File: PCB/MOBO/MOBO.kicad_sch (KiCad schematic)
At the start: 5 parts, among them J103 RPi_GPio, J104 RPi_GND, J105 RPi_5V, J106 RPi_DM, J107 RPi_DM

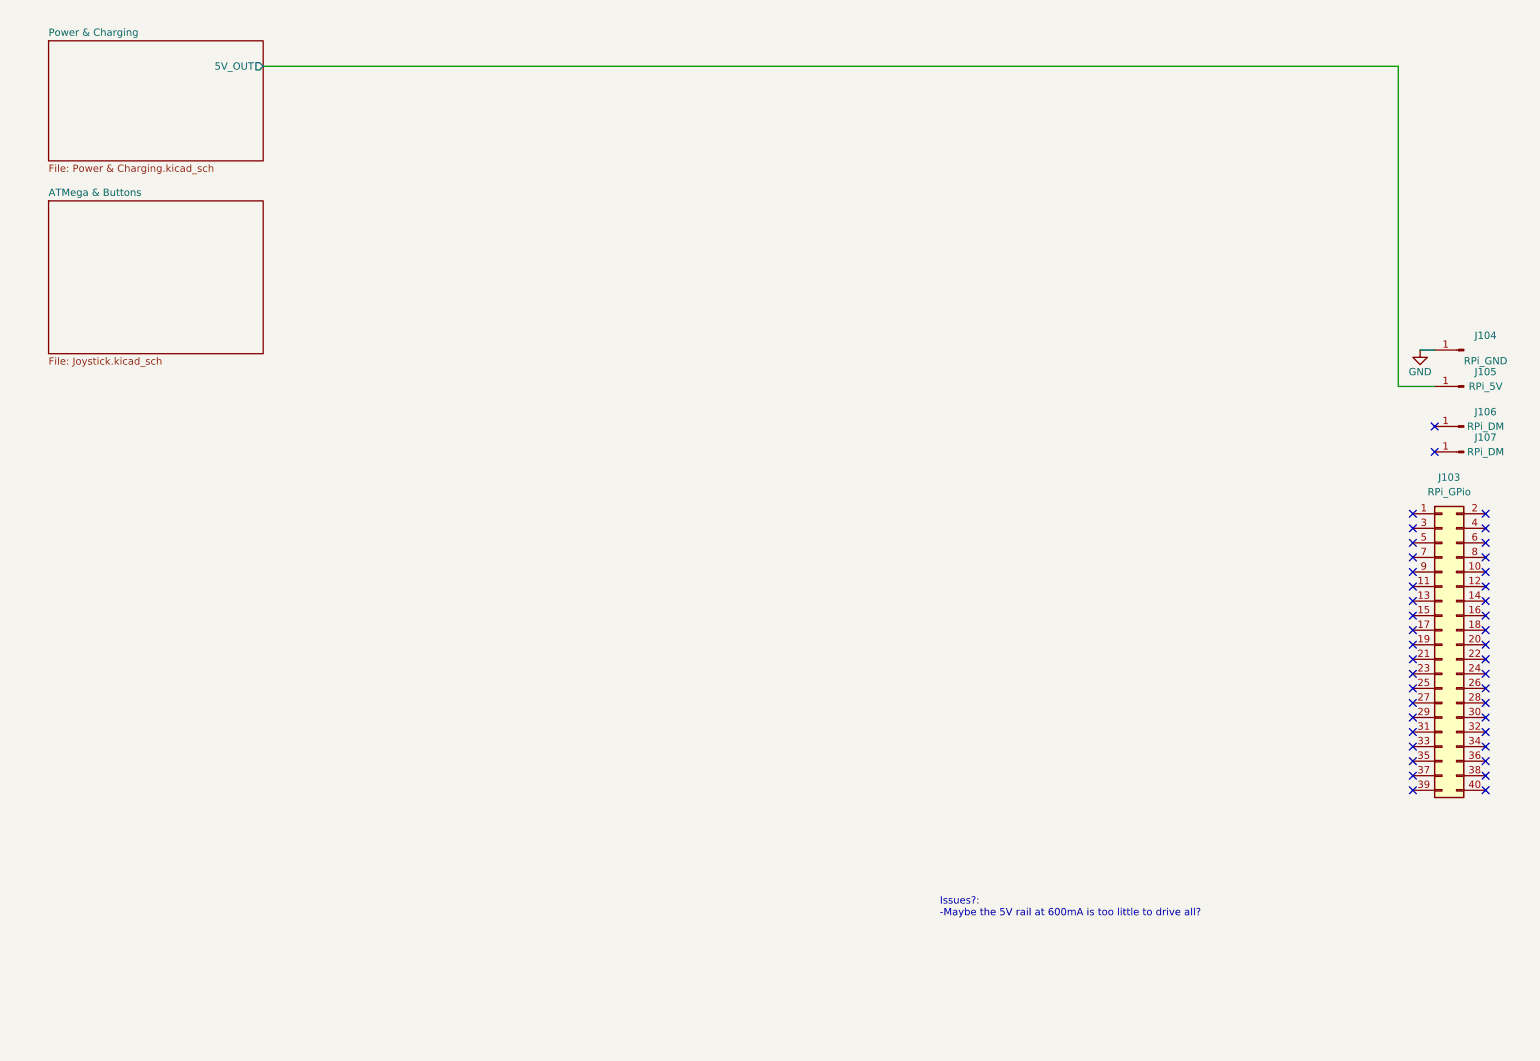
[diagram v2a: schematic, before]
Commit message: added all joystick buttons
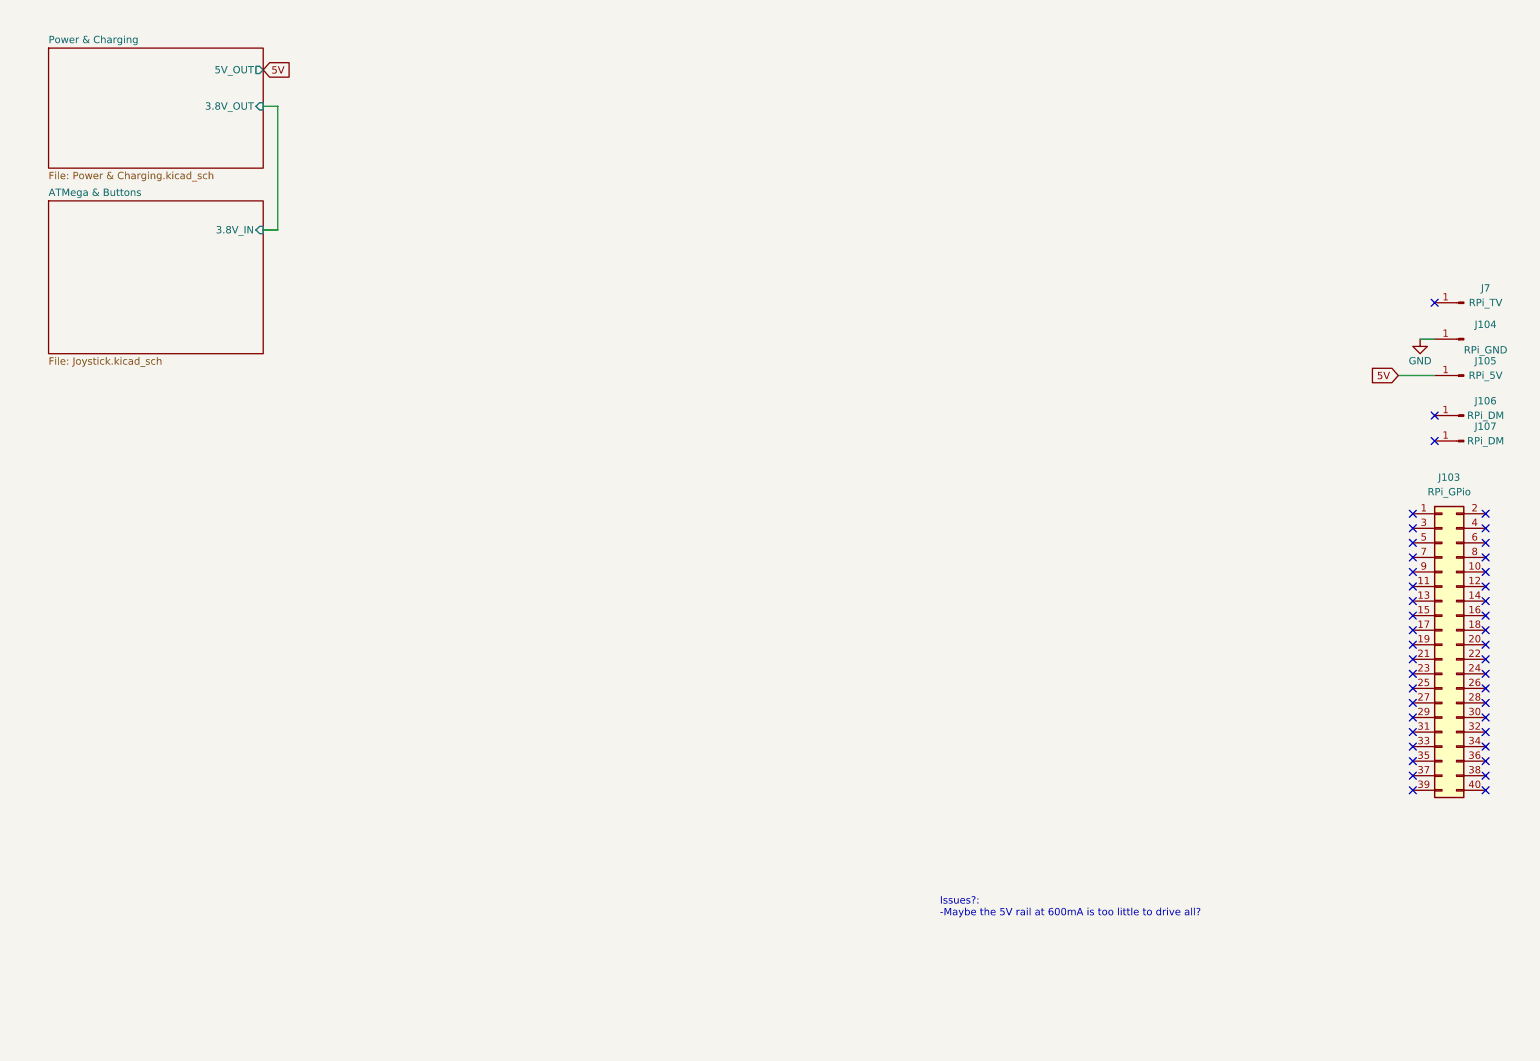
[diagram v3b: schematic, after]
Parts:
- added J7: RPi_TV, TestPoint:TestPoint_Pad_1.5x1.5mm, symbol Connector:Conn_01x01_Male
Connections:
- net Power & Charging/5V_OUT renamed 5V
- no-connect marks 42 -> 43
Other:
- sheet ATMega & Buttons ports: added 3.8V_IN; removed none
- sheet Power & Charging ports: added 3.8V_OUT; removed none
- moved on the sheet: J104, J105, J106, J107
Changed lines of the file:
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@@
   (no_connect (at 260.35 107.95))
   (no_connect (at 260.35 135.89))
-  (no_connect (at 264.16 89.535))
+  (no_connect (at 264.16 87.63))
   (no_connect (at 273.05 135.89))
   (no_connect (at 260.35 125.73))
@@
   (no_connect (at 260.35 146.05))
   (no_connect (at 260.35 113.03))
-  (no_connect (at 264.16 85.09))
+  (no_connect (at 264.16 83.185))
   (no_connect (at 260.35 143.51))
   (no_connect (at 260.35 140.97))
@@
   (no_connect (at 273.05 120.65))
   (no_connect (at 260.35 102.87))
+  (no_connect (at 264.16 63.5))
   (no_connect (at 273.05 140.97))
   (no_connect (at 260.35 115.57))
@@
   (no_connect (at 273.05 148.59))
   (no_connect (at 273.05 102.87))
-  (wire (pts (xy 257.81 22.225) (xy 257.81 78.105))
-    (stroke (width 0) (type default))
-  )
-  (wire (pts (xy 261.62 71.755) (xy 264.16 71.755))
-    (stroke (width 0) (type default))
-  )
-  (wire (pts (xy 59.69 22.225) (xy 257.81 22.225))
-    (stroke (width 0) (type default))
-  )
-  (wire (pts (xy 257.81 78.105) (xy 264.16 78.105))
+  (wire (pts (xy 59.69 29.21) (xy 62.23 29.21))
+    (stroke (width 0) (type default))
+  )
+  (wire (pts (xy 62.23 50.8) (xy 59.69 50.8))
+    (stroke (width 0) (type default))
+  )
+  (wire (pts (xy 261.62 69.85) (xy 264.16 69.85))
+    (stroke (width 0) (type default))
+  )
+  (wire (pts (xy 62.23 29.21) (xy 62.23 50.8))
+    (stroke (width 0) (type default))
+  )
+  (wire (pts (xy 257.81 76.2) (xy 264.16 76.2))
     (stroke (width 0) (type default))
   )
@@
     (at 177.8 170.815 0)
     (effects (font (size 1.27 1.27)) (justify left bottom))
+  )
+  (global_label "5V" (shape input) (at 59.69 22.86 0) (fields_autoplaced)
+    (effects (font (size 1.27 1.27)) (justify left))
+    (property "Intersheetrefs" "${INTERSHEET_REFS}" (at 64.9733 22.86 0)
+      (effects (font (size 1.27 1.27)) (justify left) hide)
+    )
+  )
+  (global_label "5V" (shape input) (at 257.81 76.2 180) (fields_autoplaced)
+    (effects (font (size 1.27 1.27)) (justify right))
+    (property "Intersheetrefs" "${INTERSHEET_REFS}" (at 252.5267 76.2 0)
+      (effects (font (size 1.27 1.27)) (justify right) hide)
+    )
+  )
+  (symbol (lib_id "Connector:Conn_01x01_Male") (at 269.24 63.5 180) (unit 1)
+    (in_bom yes) (on_board yes) (dnp no)
+    (property "Reference" "J7" (at 273.05 60.96 0)
+      (effects (font (size 1.27 1.27)))
+    )
+    (property "Value" "RPi_TV" (at 273.05 63.5 0)
+      (effects (font (size 1.27 1.27)))
+    )
+    (property "Footprint" "TestPoint:TestPoint_Pad_1.5x1.5mm" (at 269.24 63.5 0)
+      (effects (font (size 1.27 1.27)) hide)
+    )
+    (property "Datasheet" "~" (at 269.24 63.5 0)
+      (effects (font (size 1.27 1.27)) hide)
+    )
+    (pin "1")
+    (instances
+      (project "MOBO"
+        (path "/2d62a3c1-c4f2-4921-9f6b-8dc8aef69d64"
+          (reference "J7") (unit 1)
+        )
+      )
+    )
   )
   (symbol (lib_id "Connector_Generic:Conn_02x20_Odd_Even") (at 265.43 123.19 0) (unit 1)
@@
     )
   )
-  (symbol (lib_id "Connector:Conn_01x01_Male") (at 269.24 71.755 180) (unit 1)
-    (in_bom yes) (on_board yes) (dnp no)
-    (property "Reference" "J104" (at 273.05 69.215 0)
-      (effects (font (size 1.27 1.27)))
-    )
-    (property "Value" "RPi_GND" (at 273.05 73.66 0)
-      (effects (font (size 1.27 1.27)))
-    )
-    (property "Footprint" "TestPoint:TestPoint_Pad_1.5x1.5mm" (at 269.24 71.755 0)
-      (effects (font (size 1.27 1.27)) hide)
-    )
-    (property "Datasheet" "~" (at 269.24 71.755 0)
+  (symbol (lib_id "Connector:Conn_01x01_Male") (at 269.24 69.85 180) (unit 1)
+    (in_bom yes) (on_board yes) (dnp no)
+    (property "Reference" "J104" (at 273.05 67.31 0)
+      (effects (font (size 1.27 1.27)))
+    )
+    (property "Value" "RPi_GND" (at 273.05 71.755 0)
+      (effects (font (size 1.27 1.27)))
+    )
+    (property "Footprint" "TestPoint:TestPoint_Pad_1.5x1.5mm" (at 269.24 69.85 0)
+      (effects (font (size 1.27 1.27)) hide)
+    )
+    (property "Datasheet" "~" (at 269.24 69.85 0)
       (effects (font (size 1.27 1.27)) hide)
     )
@@
     )
   )
-  (symbol (lib_id "Connector:Conn_01x01_Male") (at 269.24 89.535 180) (unit 1)
-    (in_bom yes) (on_board yes) (dnp no)
-    (property "Reference" "J107" (at 273.05 86.995 0)
-      (effects (font (size 1.27 1.27)))
-    )
-    (property "Value" "RPi_DM" (at 273.05 89.535 0)
-      (effects (font (size 1.27 1.27)))
-    )
-    (property "Footprint" "TestPoint:TestPoint_Pad_1.5x1.5mm" (at 269.24 89.535 0)
-      (effects (font (size 1.27 1.27)) hide)
-    )
-    (property "Datasheet" "~" (at 269.24 89.535 0)
+  (symbol (lib_id "Connector:Conn_01x01_Male") (at 269.24 87.63 180) (unit 1)
+    (in_bom yes) (on_board yes) (dnp no)
+    (property "Reference" "J107" (at 273.05 85.09 0)
+      (effects (font (size 1.27 1.27)))
+    )
+    (property "Value" "RPi_DM" (at 273.05 87.63 0)
+      (effects (font (size 1.27 1.27)))
+    )
+    (property "Footprint" "TestPoint:TestPoint_Pad_1.5x1.5mm" (at 269.24 87.63 0)
+      (effects (font (size 1.27 1.27)) hide)
+    )
+    (property "Datasheet" "~" (at 269.24 87.63 0)
       (effects (font (size 1.27 1.27)) hide)
     )
@@
     )
   )
-  (symbol (lib_id "Connector:Conn_01x01_Male") (at 269.24 85.09 180) (unit 1)
-    (in_bom yes) (on_board yes) (dnp no)
-    (property "Reference" "J106" (at 273.05 82.55 0)
-      (effects (font (size 1.27 1.27)))
-    )
-    (property "Value" "RPi_DM" (at 273.05 85.09 0)
-      (effects (font (size 1.27 1.27)))
-    )
-    (property "Footprint" "TestPoint:TestPoint_Pad_1.5x1.5mm" (at 269.24 85.09 0)
-      (effects (font (size 1.27 1.27)) hide)
-    )
-    (property "Datasheet" "~" (at 269.24 85.09 0)
+  (symbol (lib_id "Connector:Conn_01x01_Male") (at 269.24 83.185 180) (unit 1)
+    (in_bom yes) (on_board yes) (dnp no)
+    (property "Reference" "J106" (at 273.05 80.645 0)
+      (effects (font (size 1.27 1.27)))
+    )
+    (property "Value" "RPi_DM" (at 273.05 83.185 0)
+      (effects (font (size 1.27 1.27)))
+    )
+    (property "Footprint" "TestPoint:TestPoint_Pad_1.5x1.5mm" (at 269.24 83.185 0)
+      (effects (font (size 1.27 1.27)) hide)
+    )
+    (property "Datasheet" "~" (at 269.24 83.185 0)
       (effects (font (size 1.27 1.27)) hide)
     )
@@
     )
   )
-  (symbol (lib_id "Connector:Conn_01x01_Male") (at 269.24 78.105 180) (unit 1)
-    (in_bom yes) (on_board yes) (dnp no)
-    (property "Reference" "J105" (at 273.05 75.565 0)
-      (effects (font (size 1.27 1.27)))
-    )
-    (property "Value" "RPi_5V" (at 273.05 78.105 0)
-      (effects (font (size 1.27 1.27)))
-    )
-    (property "Footprint" "TestPoint:TestPoint_Pad_1.5x1.5mm" (at 269.24 78.105 0)
-      (effects (font (size 1.27 1.27)) hide)
-    )
-    (property "Datasheet" "~" (at 269.24 78.105 0)
+  (symbol (lib_id "Connector:Conn_01x01_Male") (at 269.24 76.2 180) (unit 1)
+    (in_bom yes) (on_board yes) (dnp no)
+    (property "Reference" "J105" (at 273.05 73.66 0)
+      (effects (font (size 1.27 1.27)))
+    )
+    (property "Value" "RPi_5V" (at 273.05 76.2 0)
+      (effects (font (size 1.27 1.27)))
+    )
+    (property "Footprint" "TestPoint:TestPoint_Pad_1.5x1.5mm" (at 269.24 76.2 0)
+      (effects (font (size 1.27 1.27)) hide)
+    )
+    (property "Datasheet" "~" (at 269.24 76.2 0)
       (effects (font (size 1.27 1.27)) hide)
     )
@@
     )
   )
-  (symbol (lib_id "power:GND") (at 261.62 71.755 0) (unit 1)
-    (in_bom yes) (on_board yes) (dnp no)
-    (property "Reference" "#PWR0102" (at 261.62 78.105 0)
-      (effects (font (size 1.27 1.27)) hide)
-    )
-    (property "Value" "GND" (at 261.62 75.565 0)
-      (effects (font (size 1.27 1.27)))
-    )
-    (property "Footprint" "" (at 261.62 71.755 0)
-      (effects (font (size 1.27 1.27)) hide)
-    )
-    (property "Datasheet" "" (at 261.62 71.755 0)
+  (symbol (lib_id "power:GND") (at 261.62 69.85 0) (unit 1)
+    (in_bom yes) (on_board yes) (dnp no)
+    (property "Reference" "#PWR0102" (at 261.62 76.2 0)
+      (effects (font (size 1.27 1.27)) hide)
+    )
+    (property "Value" "GND" (at 261.62 73.66 0)
+      (effects (font (size 1.27 1.27)))
+    )
+    (property "Footprint" "" (at 261.62 69.85 0)
+      (effects (font (size 1.27 1.27)) hide)
+    )
+    (property "Datasheet" "" (at 261.62 69.85 0)
       (effects (font (size 1.27 1.27)) hide)
     )
@@
       (effects (font (size 1.27 1.27)) (justify left top))
     )
+    (pin "3.8V_IN" input (at 59.69 50.8 0)
+      (effects (font (size 1.27 1.27)) (justify right))
+    )
     (instances
       (project "MOBO"
@@
     )
   )
-  (sheet (at 22.225 17.78) (size 37.465 20.955) (fields_autoplaced)
+  (sheet (at 22.225 19.05) (size 37.465 20.955) (fields_autoplaced)
     (stroke (width 0.1524) (type solid))
     (fill (color 0 0 0 0.0000))
-    (property "Sheetname" "Power & Charging" (at 22.225 17.0684 0)
+    (property "Sheetname" "Power & Charging" (at 22.225 18.3384 0)
       (effects (font (size 1.27 1.27)) (justify left bottom))
     )
-    (property "Sheetfile" "Power & Charging.kicad_sch" (at 22.225 39.3196 0)
+    (property "Sheetfile" "Power & Charging.kicad_sch" (at 22.225 40.5896 0)
       (effects (font (size 1.27 1.27)) (justify left top))
     )
-    (pin "5V_OUT" output (at 59.69 22.225 0)
+    (pin "5V_OUT" output (at 59.69 22.86 0)
       (effects (font (size 1.27 1.27)) (justify right))
     )
+    (pin "3.8V_OUT" input (at 59.69 29.21 0)
+      (effects (font (size 1.27 1.27)) (justify right))
+    )
